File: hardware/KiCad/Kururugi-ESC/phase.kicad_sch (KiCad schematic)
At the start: 21 parts, among them J9 Conn_01x01, Q1 CSD18540Q5B, Q2 CSD18540Q5B, U4 2EDL8024

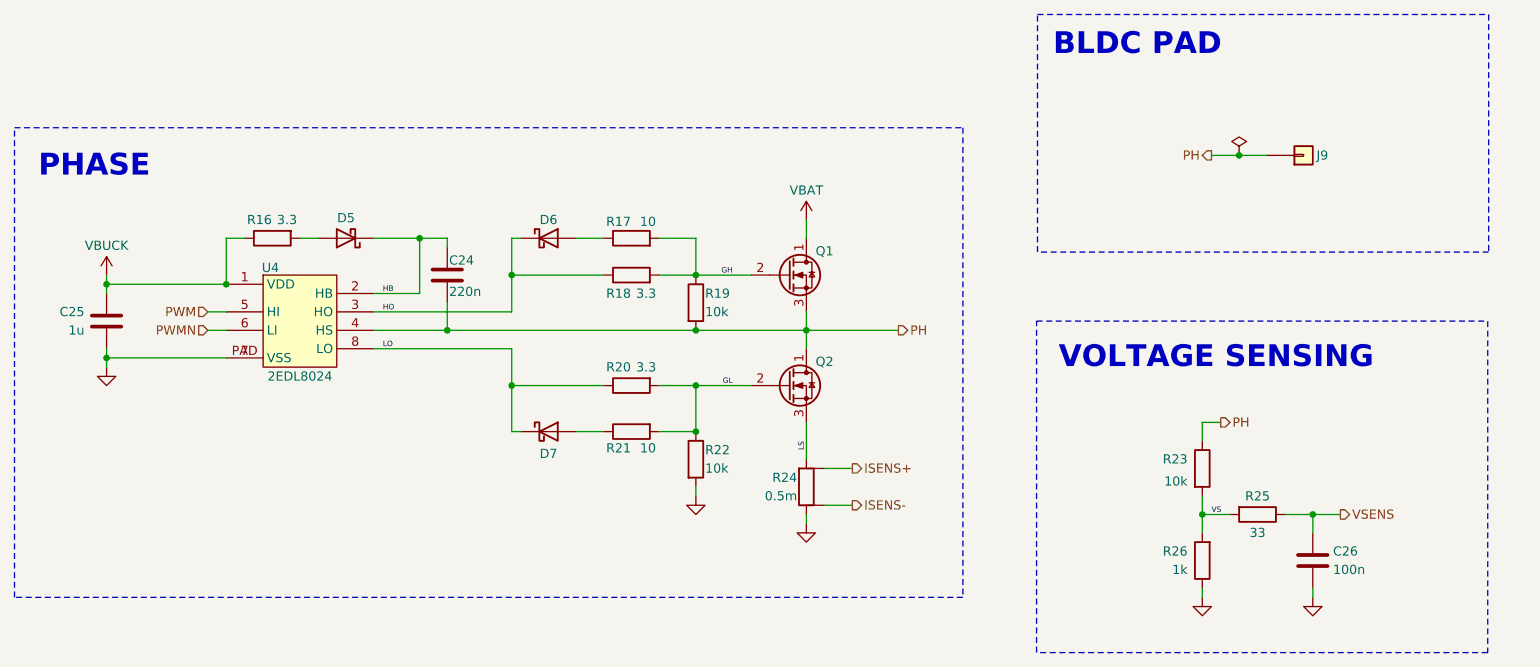
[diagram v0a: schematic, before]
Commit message: Doc Update + Added CubeIDE
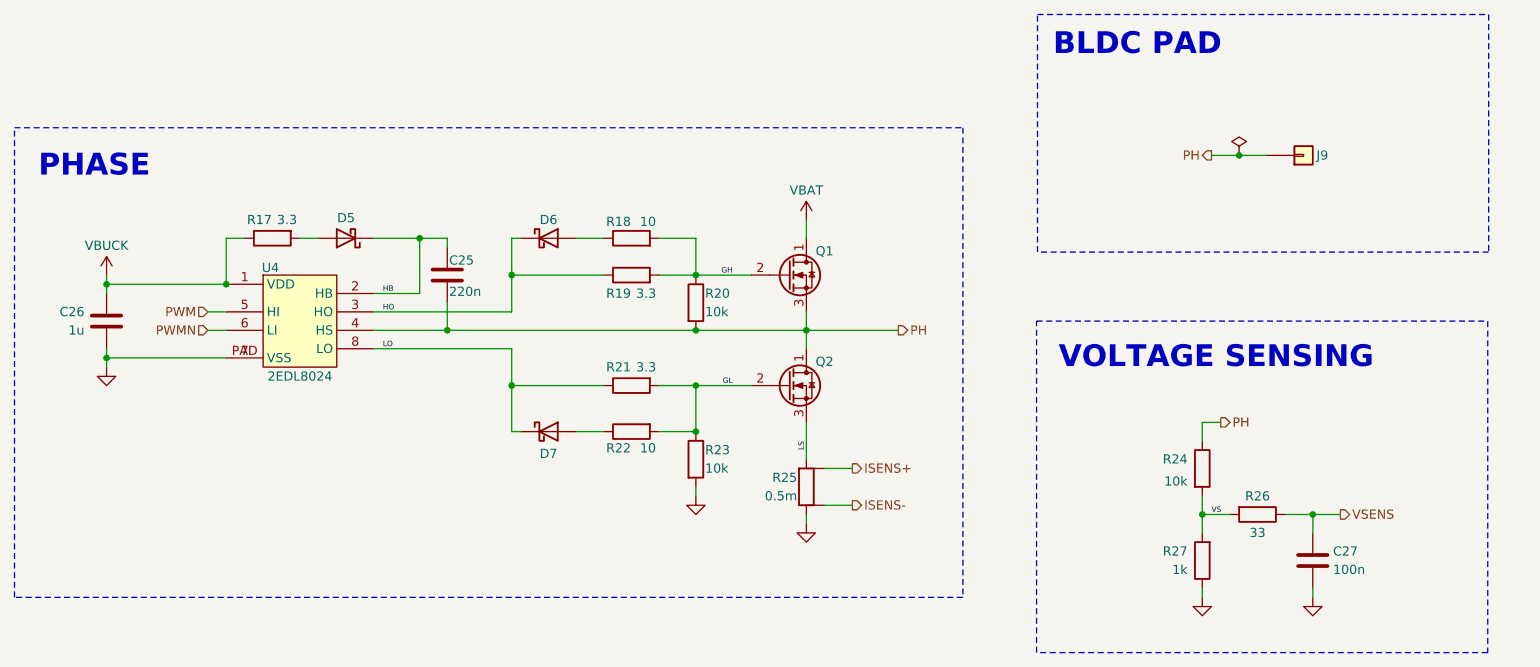
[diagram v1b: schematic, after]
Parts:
- renumbered C24 to C25, C25 to C26, C26 to C27, R16 to R17, R17 to R18, R18 to R19, R19 to R20, R20 to R21, R21 to R22, R22 to R23, R23 to R24, R24 to R25, R25 to R26, R26 to R27

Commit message: Kicad minor corrections
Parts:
- R26: LCSC C25752 -> C25105
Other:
- moved on the sheet: C25, C26, C27, D5, D6, D7, J9, Q1, Q2, R17, R18, R19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
